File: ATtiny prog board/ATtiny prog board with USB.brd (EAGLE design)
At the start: 17.8 x 24.1 mm, 11 parts, among them J1 CON_HEADER_1X06-PTH

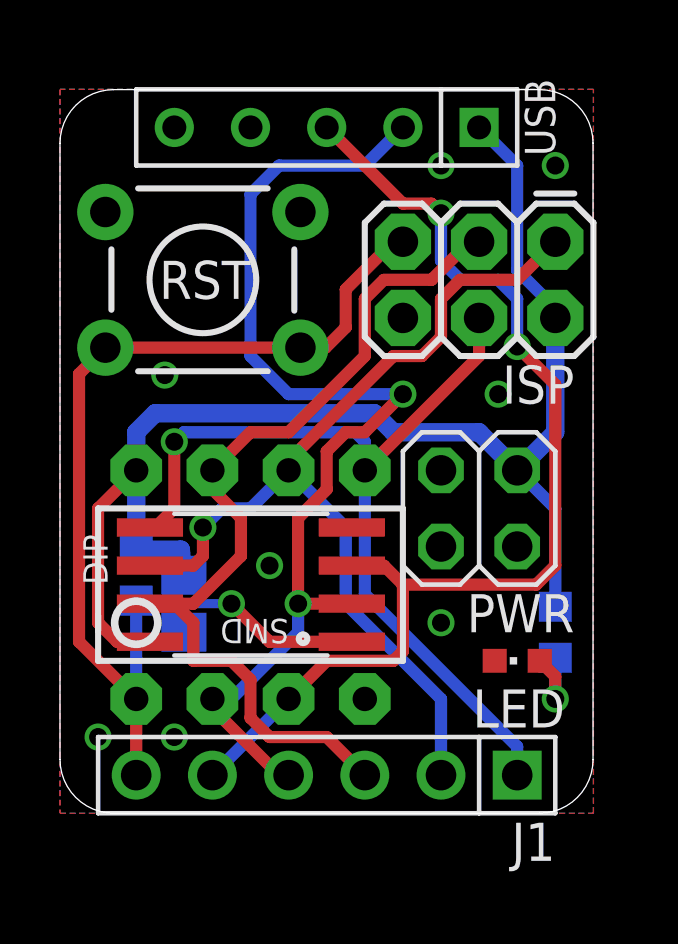
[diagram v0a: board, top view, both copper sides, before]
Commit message: added some info to silk screen
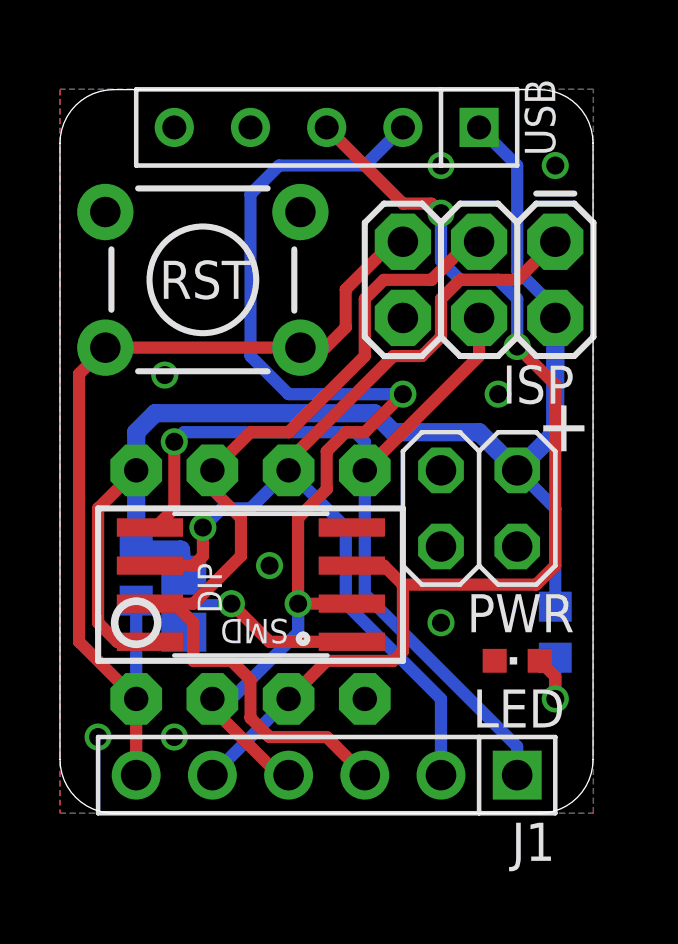
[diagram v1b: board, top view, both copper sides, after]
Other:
- board text added: "+"
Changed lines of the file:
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@@
 <wire x1="15.987359375" y1="24.12" x2="1.78899375" y2="24.12" width="0" layer="20"/>
 <wire x1="1.78899375" y1="24.12" x2="0" y2="22.33100625" width="0" layer="20" curve="90"/>
+<text x="15.875" y="12.065" size="1.778" layer="25">+</text>
 </plain>
 <attributes>
@@
 <attribute name="PROD_ID" value="IC-09445" x="6.35" y="7.62" size="1.778" layer="27" display="off"/>
 <attribute name="VALUE" x="3.175" y="6.985" size="1.27" layer="27" ratio="10"/>
-<attribute name="NAME" x="1.5875" y="7.62" size="0.8128" layer="25" ratio="10" rot="R90"/>
+<attribute name="NAME" x="5.3975" y="6.6675" size="0.8128" layer="25" ratio="10" rot="R90"/>
 </element>
 <element name="ISP" library="SparkFun-Connectors" package="2X3" value="" x="16.51" y="19.05" smashed="yes" rot="R180">

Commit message: updated ATtiny prog board with USB
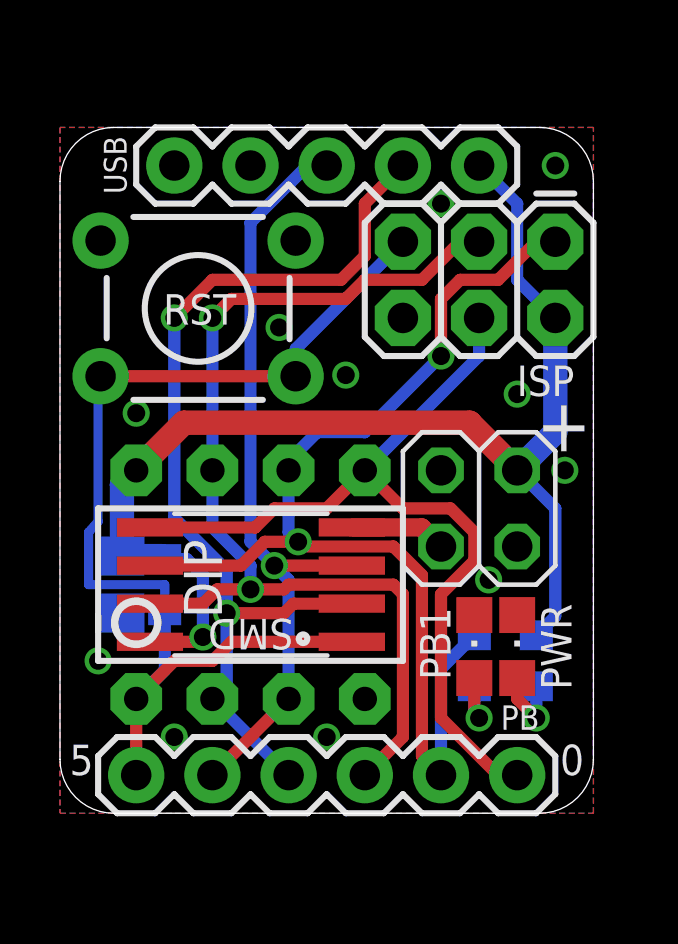
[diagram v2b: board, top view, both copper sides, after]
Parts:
- removed J1: CON_HEADER_1X06-PTH, dp_devices:M1X6
- removed LED: (no value), dp_devices:LED-603
- added PB: (no value), SparkFun-Connectors:1X06
- added PB1, PWR_LED: (no value), dp_devices:LED-805
- added R3: 300, dp_devices:R603
- USB: value CON_HEADER_1X05-PTH -> (none); device dp_devices:M1X5 -> SparkFun-Connectors:1X05
- moved USB 5.24 mm to (14.0, 21.6)
- moved C1 2.16 mm to (2.06, 7.62)
- moved R2 1.14 mm to (15.9, 5.08)
- moved R1 1.00 mm to (3.49, 7.62)
- moved RST 0.97 mm to (4.60, 16.8)
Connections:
- new net N$2: PB1.A, R3.2
- net GND: now also PB1.C, PWR_LED.C; no longer LED.C
- net N$1: now also PWR_LED.A; no longer LED.A
- net PB0/MOSI: now also PB.1; no longer J1.1
- net PB1/MISO: now also PB.2, R3.1; no longer J1.2
- net PB2/SCK: now also PB.3; no longer J1.3
- net PB3/D-: now also PB.4; no longer J1.4
- net PB4/D+: now also PB.5; no longer J1.5
- net PB5/RST: now also PB.6; no longer J1.6
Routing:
- net PB4/D+: track 36.7 -> 25.9 mm, vias 2 -> 1
- net PB1/MISO: track 31.7 -> 37.8 mm, vias 1 -> 2
- net PB2/SCK: track 30.3 -> 34.9 mm, vias 0 -> 2
- net PB3/D-: track 36.1 -> 32.3 mm
- net VDD: track 45.7 -> 42.0 mm, vias 0 -> 1
- net GND: track 0.00 -> 3.23 mm, vias 8 -> 11
- net N$2: track 0.00 -> 2.52 mm, vias 0 -> 1
- net PB5/RST: track 38.6 -> 36.8 mm, vias 1 -> 0
- net PB0/MOSI: track 29.8 -> 29.1 mm, vias 1 -> 0
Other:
- board size 17.8 x 24.1 mm -> 17.8 x 22.9 mm
- board text added: "0"
- board text added: "5"
